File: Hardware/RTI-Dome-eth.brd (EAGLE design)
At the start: 119.4 x 71.1 mm, 78 parts, among them IC1 24AA128ST, IC3 FT232RL, IC5 74LVC245, IC6 74ABT245, J1 POWERPOLE_POWER45A, U1 W5500, X13 PN61729-S, X9 J1011F21PNL

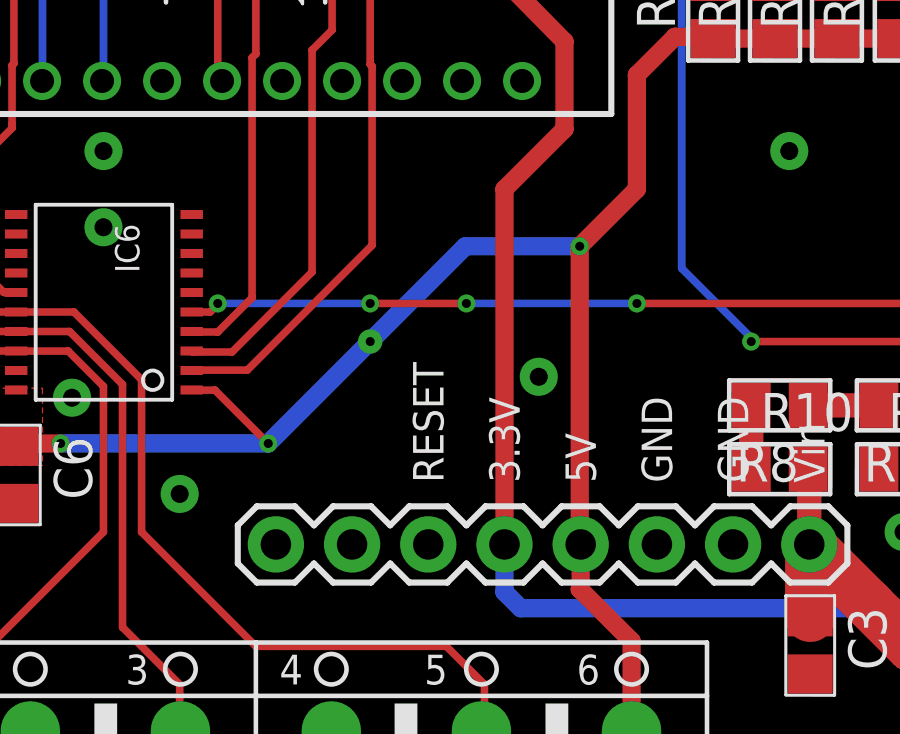
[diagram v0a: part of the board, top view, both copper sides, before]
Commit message: Adding MCP120 for power on reset.
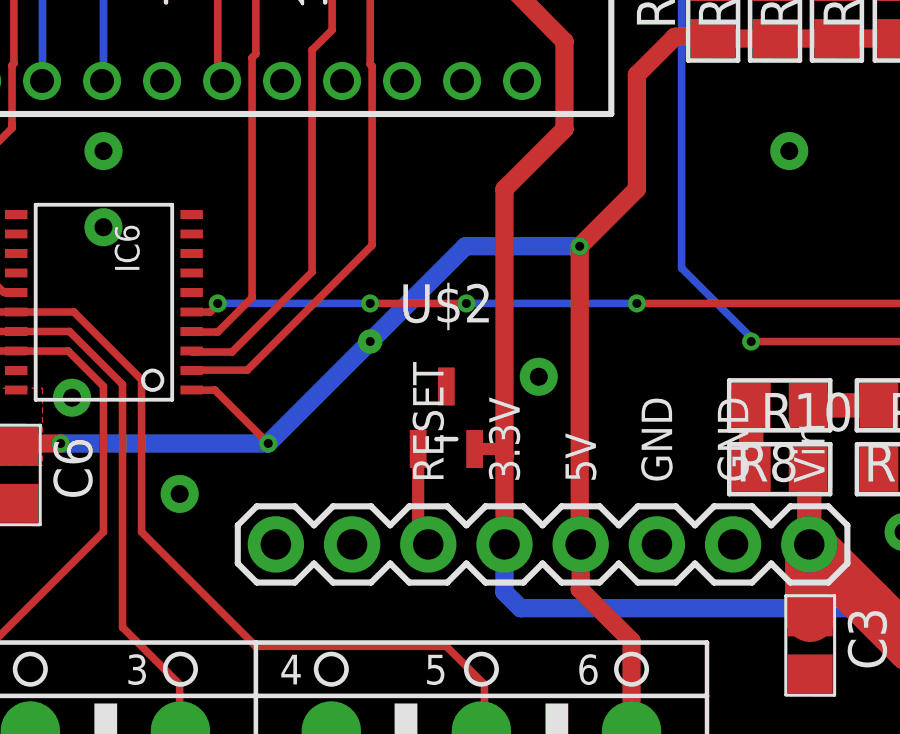
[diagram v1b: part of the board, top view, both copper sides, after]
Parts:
- added U$2: MCP120T-270I_TT, MCP120T-270I_TT:SOT95P237X112-3N
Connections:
- new net RESET: U$1.RESET, U$2.1
- net 3.3V: now also U$2.2
- net GND: now also U$2.3
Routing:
- net RESET: track 0.00 -> 3.32 mm
- net 3.3V: track 350.8 -> 351.9 mm
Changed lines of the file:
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@@
 <layer number="49" name="Reference" color="7" fill="1" visible="yes" active="yes"/>
 <layer number="50" name="dxf" color="7" fill="1" visible="no" active="no"/>
-<layer number="51" name="tDocu" color="7" fill="1" visible="no" active="yes"/>
+<layer number="51" name="tDocu" color="7" fill="1" visible="yes" active="yes"/>
 <layer number="52" name="bDocu" color="7" fill="1" visible="yes" active="yes"/>
 <layer number="53" name="tGND_GNDA" color="7" fill="9" visible="no" active="no"/>
@@
 <element name="C20" library="rti" package="C0805" value="100nF" x="53.34" y="27.94" rot="R90"/>
 <element name="R30" library="rti" package="R0805" value="4.7K" x="58.83275" y="22.86" rot="R270"/>
+<element name="U$2" library="MCP120T-270I_TT" package="SOT95P237X112-3N" value="MCP120T-270I_TT" x="22.86" y="15.24">
+<attribute name="MANUFACTURER_PART_NUMBER" value="MCP120T-270I/TT" x="10.16" y="25.4" size="1.778" layer="27" display="off"/>
+<attribute name="MANUFACTURER_NAME" value="Microchip" x="10.16" y="25.4" size="1.778" layer="27" display="off"/>
+<attribute name="MOUSER_PART_NUMBER" value="579-MCP120T-270I/TT" x="10.16" y="25.4" size="1.778" layer="27" display="off"/>
+<attribute name="DESCRIPTION" value="Microcontroller Supervisory Circuit" x="10.16" y="25.4" size="1.778" layer="27" display="off"/>
+<attribute name="HEIGHT" value="mm" x="10.16" y="25.4" size="1.778" layer="27" display="off"/>
+<attribute name="MOUSER_PRICE-STOCK" value="https://www.mouser.co.uk/ProductDetail/Microchip-Technology/MCP120T-270I-TT?qs=JaP0%252BruNJH91Pwyk6aJdSA%3D%3D" x="10.16" y="25.4" size="1.778" layer="27" display="off"/>
+</element>
 </elements>
 <signals>
@@
 <via x="91.44" y="48.26" extent="1-16" drill="0.6" diameter="1.27"/>
 <via x="91.44" y="44.45" extent="1-16" drill="0.6" diameter="1.27"/>
+<contactref element="U$2" pad="3"/>
 </signal>
 <signal name="+12V" class="1">
@@
 <wire x1="67.33" y1="40.94" x2="67.31" y2="40.96" width="0.254" layer="1"/>
 <wire x1="26.797" y1="24.86025" x2="24.79675" y2="22.86" width="0.6096" layer="1"/>
-<wire x1="24.79675" y1="22.86" x2="24.79675" y2="11.01725" width="0.6096" layer="1"/>
+<wire x1="24.79675" y1="22.86" x2="24.79675" y2="13.97" width="0.6096" layer="1"/>
+<wire x1="24.79675" y1="13.97" x2="24.79675" y2="11.01725" width="0.6096" layer="1"/>
 <wire x1="95.57" y1="24.41575" x2="92.42425" y2="24.41575" width="0.6096" layer="1"/>
 <wire x1="92.42425" y1="24.41575" x2="91.44" y2="25.4" width="0.6096" layer="1"/>
@@
 <wire x1="58.83275" y1="21.91" x2="56.2" y2="21.91" width="0.4064" layer="1"/>
 <wire x1="56.2" y1="21.91" x2="55.88" y2="21.59" width="0.4064" layer="1"/>
+<contactref element="U$2" pad="2"/>
+<wire x1="23.7998" y1="14.1986" x2="24.56815" y2="14.1986" width="0.4064" layer="1"/>
+<wire x1="24.56815" y1="14.1986" x2="24.79675" y2="13.97" width="0.4064" layer="1"/>
 </signal>
 <signal name="RG-11-IN_5V">
@@
 <wire x1="58.1" y1="23.81" x2="58.83275" y2="23.81" width="0.254" layer="1"/>
 </signal>
+<signal name="RESET">
+<contactref element="U$2" pad="1"/>
+<contactref element="U$1" pad="RESET"/>
+<wire x1="21.9202" y1="14.1986" x2="21.9202" y2="11.3538" width="0.4064" layer="1"/>
+<wire x1="21.9202" y1="11.3538" x2="22.25675" y2="11.01725" width="0.4064" layer="1"/>
+</signal>
 </signals>

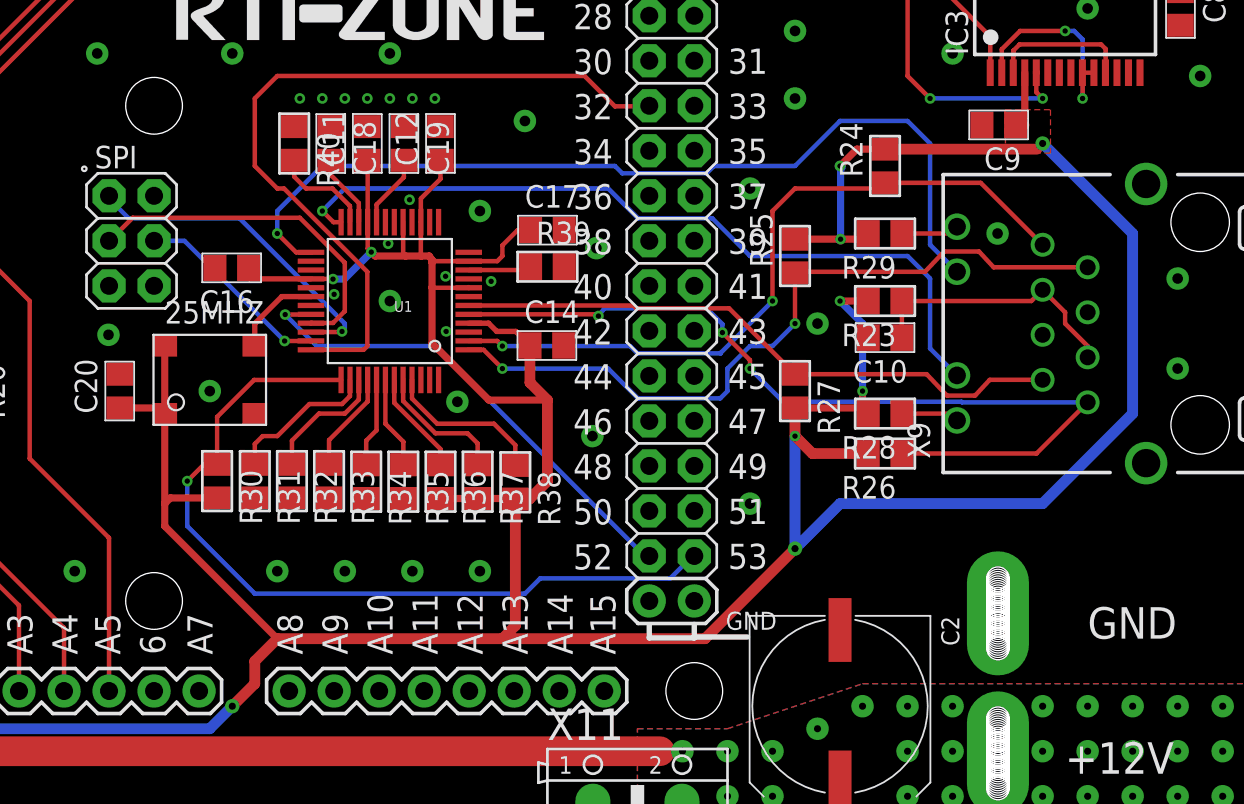
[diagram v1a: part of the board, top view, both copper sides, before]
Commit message: Redid the analog 3.3V on the ethernet shield
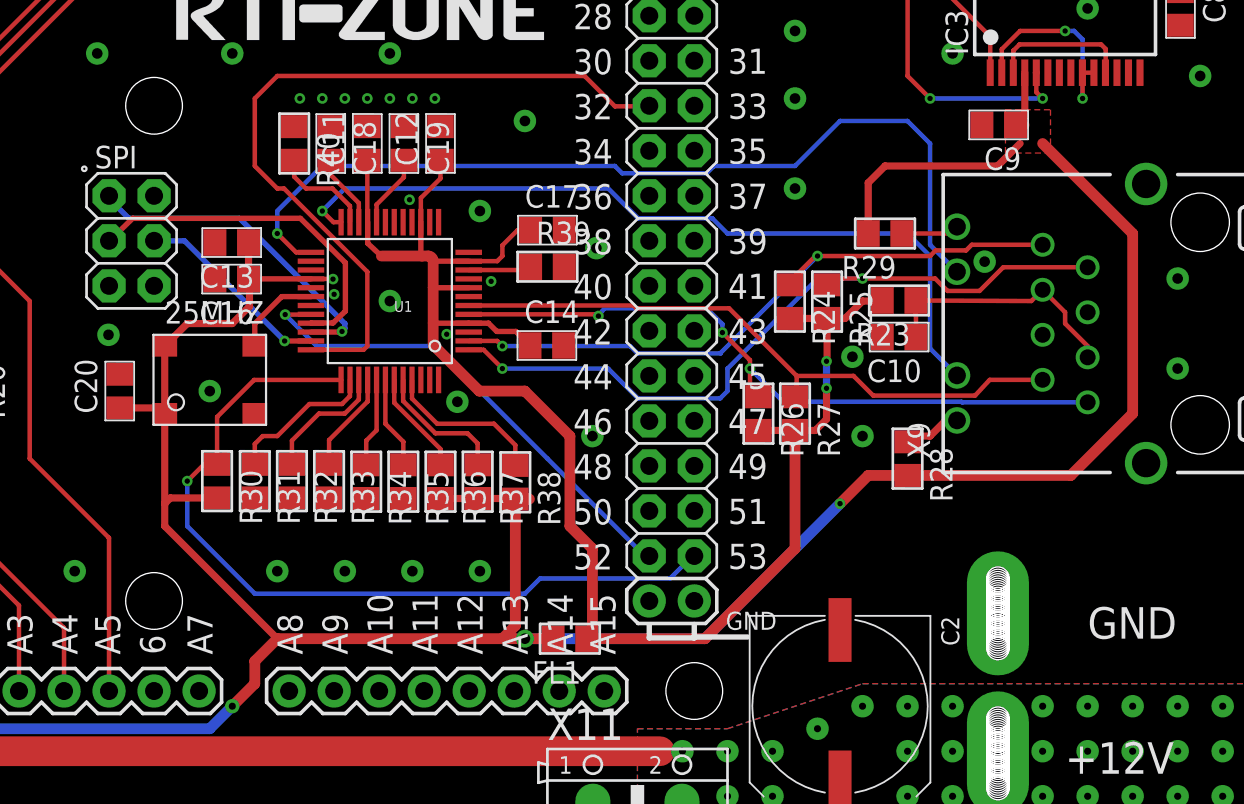
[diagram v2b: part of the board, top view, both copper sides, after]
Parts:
- added C13: 10nF, rti:C0805
- added FL1: BLM21AG121SN1D, BLM21AG121SN1D:L0805
- moved R24 9.35 mm to (91.2, 33.0), turned to 270 degrees
- moved R26 7.49 mm to (89.4, 26.7), turned to 270 degrees
- moved R25 3.14 mm to (93.2, 33.0), turned to 270 degrees
- moved R28 2.84 mm to (97.8, 24.1), turned to 270 degrees
- moved R27 1.27 mm to (91.4, 26.7)
- moved C10 0.79 mm to (97.3, 31.0)
- moved R23 0.79 mm to (97.3, 33.1)
- moved C16 0.64 mm to (59.7, 34.3)
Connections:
- new net AVDD: C11.1, C12.1, C14.1, C17.1, FL1.1, R23.2, R24.2, R25.2, R26.2, R27.2, U1.11, U1.15, U1.17, U1.21, U1.4, U1.8
- net 3.3V: now also C13.1, FL1.2; no longer C11.1, C12.1, C14.1, C17.1, R23.2, R24.2, R25.2, R26.2, R27.2, U1.11, U1.15, U1.17, U1.21, U1.4, U1.8
- net GND: now also C13.2
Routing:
- net AVDD: track 0.00 -> 91.9 mm, vias 0 -> 2
- net 3.3V: track 351.9 -> 275.5 mm, vias 10 -> 4
- net RXN: track 49.6 -> 39.8 mm
- net TXP: track 41.1 -> 37.6 mm
- net RXP: track 35.2 -> 36.1 mm
- net N$7: track 15.1 -> 14.3 mm
- net SPD_100: track 44.3 -> 45.1 mm
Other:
- board text added: "Dome Rotator"

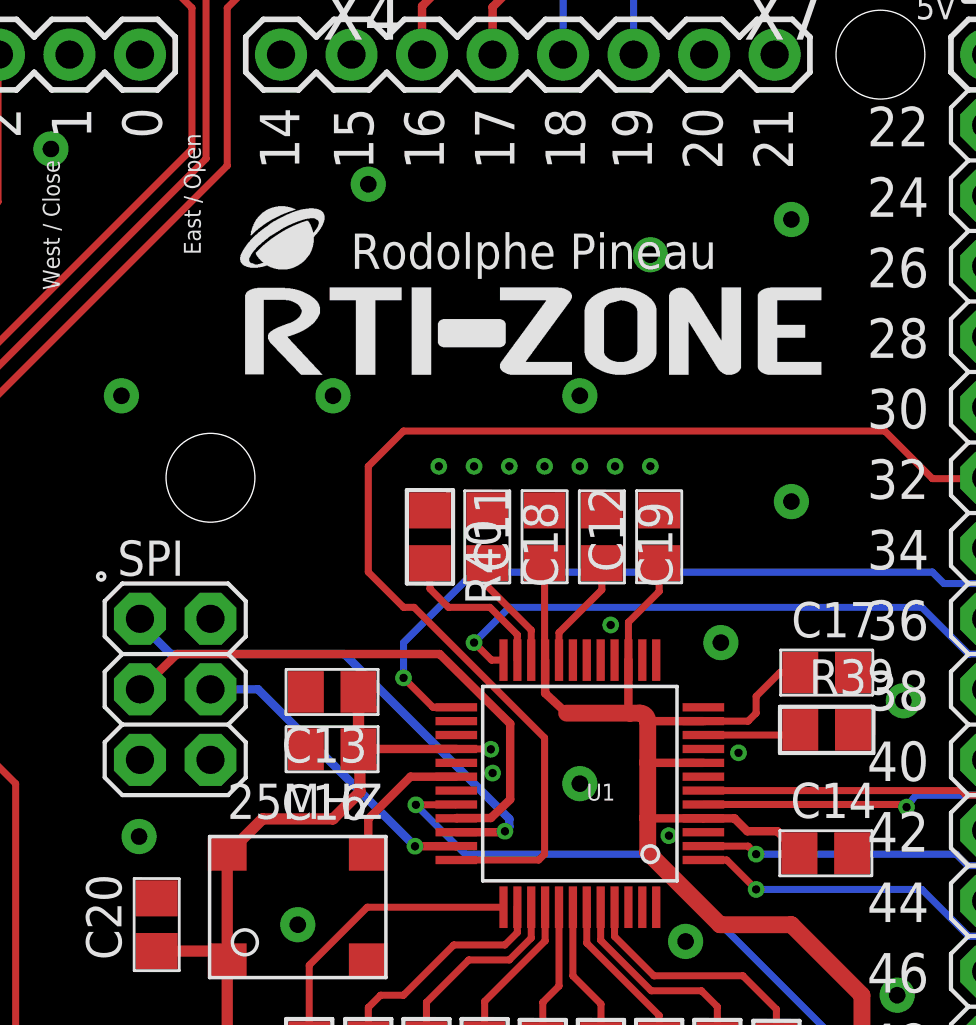
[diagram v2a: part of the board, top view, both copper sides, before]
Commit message: Fix some routing
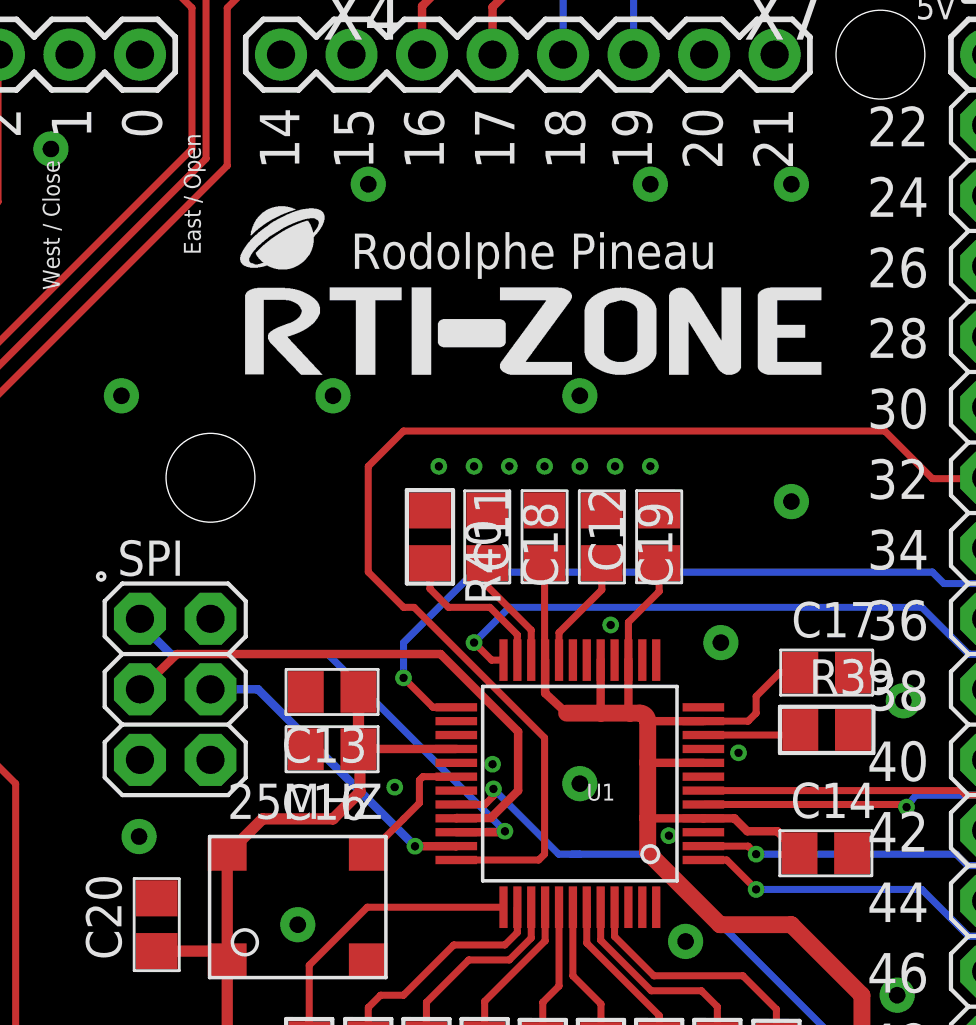
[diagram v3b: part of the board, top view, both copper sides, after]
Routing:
- net ETH_CS: track 27.6 -> 25.7 mm
- net AVDD: track 91.9 -> 93.8 mm
- net 3.3V: track 275.5 -> 274.3 mm, vias 4 -> 3
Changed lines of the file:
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@@
 <via x="52.705" y="31.115" extent="1-16" drill="0.6" diameter="1.27"/>
 <via x="69.69125" y="38.735" extent="1-16" drill="0.3"/>
-<via x="65.43675" y="33.401" extent="1-16" drill="0.3"/>
+<via x="65.43675" y="33.7185" extent="1-16" drill="0.3"/>
 <via x="63.5" y="44.45" extent="1-16" drill="0.3"/>
 <via x="66.04" y="44.45" extent="1-16" drill="0.3"/>
@@
 <via x="59.69" y="46.99" extent="1-16" drill="0.6" diameter="1.27"/>
 <via x="68.58" y="46.99" extent="1-16" drill="0.6" diameter="1.27"/>
-<via x="71.12" y="52.07" extent="1-16" drill="0.6" diameter="1.27"/>
-<via x="76.2" y="53.34" extent="1-16" drill="0.6" diameter="1.27"/>
+<via x="71.12" y="54.61" extent="1-16" drill="0.6" diameter="1.27"/>
+<via x="76.2" y="54.61" extent="1-16" drill="0.6" diameter="1.27"/>
 <via x="52.07" y="46.99" extent="1-16" drill="0.6" diameter="1.27"/>
 <via x="91.44" y="55.88" extent="1-16" drill="0.6" diameter="1.27"/>
@@
 <contactref element="C13" pad="2"/>
 <via x="71.78675" y="31.14675" extent="1-16" drill="0.3"/>
+<via x="61.9125" y="32.893" extent="1-16" drill="0.3"/>
 </signal>
 <signal name="+12V" class="1">
@@
 <contactref element="R37" pad="2"/>
 <contactref element="R36" pad="2"/>
-<wire x1="64.13" y1="34.27" x2="65.298" y2="34.27" width="0.254" layer="1"/>
-<wire x1="65.298" y1="34.27" x2="65.37325" y2="34.25825" width="0.3048" layer="1"/>
-<via x="65.37325" y="34.25825" extent="1-16" drill="0.3"/>
 <wire x1="75.66025" y1="21.8465" x2="75.66025" y2="14.70025" width="0.6096" layer="1"/>
 <wire x1="75.66025" y1="14.70025" x2="74.93" y2="13.97" width="0.6096" layer="1"/>
@@
 <wire x1="52.73675" y1="38.95725" x2="52.73675" y2="38.7985" width="0.3048" layer="16"/>
 <wire x1="52.73675" y1="38.7985" x2="53.848" y2="37.68725" width="0.3048" layer="16"/>
-<wire x1="53.848" y1="37.68725" x2="60.10275" y2="37.68725" width="0.3048" layer="16"/>
-<wire x1="60.10275" y1="37.68725" x2="66.04" y2="31.75" width="0.3048" layer="16"/>
-<wire x1="66.04" y1="31.75" x2="66.04" y2="31.46425" width="0.3048" layer="16"/>
-<wire x1="66.04" y1="31.46425" x2="65.88125" y2="31.3055" width="0.3048" layer="16"/>
 <wire x1="64.13" y1="31.27" x2="65.84575" y2="31.27" width="0.3048" layer="1"/>
 <wire x1="65.84575" y1="31.27" x2="65.88125" y2="31.3055" width="0.3048" layer="1"/>
 <via x="65.88125" y="31.3055" extent="1-16" drill="0.3"/>
+<wire x1="65.2145" y1="31.3055" x2="65.88125" y2="31.3055" width="0.254" layer="16"/>
+<wire x1="53.848" y1="37.68725" x2="59.4995" y2="37.68725" width="0.254" layer="16"/>
+<wire x1="59.4995" y1="37.68725" x2="65.88125" y2="31.3055" width="0.254" layer="16"/>
 </signal>
 <signal name="SCLK">
@@
 <wire x1="52.73675" y1="36.41725" x2="52.7685" y2="36.41725" width="0.3048" layer="1"/>
 <wire x1="52.7685" y1="36.41725" x2="54.07025" y2="37.68725" width="0.3048" layer="1"/>
-<wire x1="54.07025" y1="37.68725" x2="63.53175" y2="37.68725" width="0.3048" layer="1"/>
-<wire x1="66.07175" y1="32.4485" x2="65.37325" y2="31.78175" width="0.3048" layer="1"/>
+<wire x1="54.07025" y1="37.68725" x2="63.5635" y2="37.68725" width="0.3048" layer="1"/>
+<wire x1="66.3575" y1="32.766" x2="65.37325" y2="31.78175" width="0.3048" layer="1"/>
 <wire x1="65.37325" y1="31.78175" x2="64.14175" y2="31.78175" width="0.3048" layer="1"/>
 <wire x1="64.14175" y1="31.78175" x2="64.13" y2="31.77" width="0.3048" layer="1"/>
-<wire x1="66.07175" y1="32.4485" x2="66.07175" y2="35.179" width="0.3048" layer="1"/>
-<wire x1="66.07175" y1="35.179" x2="63.53175" y2="37.68725" width="0.3048" layer="1"/>
+<wire x1="66.3575" y1="32.766" x2="66.3575" y2="34.89325" width="0.3048" layer="1"/>
+<wire x1="66.3575" y1="34.89325" x2="63.5635" y2="37.68725" width="0.3048" layer="1"/>
 </signal>
 <signal name="SDO">
@@
 <wire x1="82.96275" y1="18.63725" x2="77.47" y2="24.13" width="0.254" layer="16"/>
 <wire x1="77.47" y1="24.13" x2="71.12" y2="30.48" width="0.254" layer="16"/>
-<wire x1="71.12" y1="30.48" x2="64.77" y2="30.48" width="0.254" layer="16"/>
-<wire x1="64.77" y1="30.48" x2="64.4525" y2="30.48" width="0.254" layer="16"/>
-<wire x1="64.4525" y1="30.48" x2="62.6745" y2="32.258" width="0.254" layer="16"/>
-<via x="62.6745" y="32.258" extent="1-16" drill="0.3"/>
-<wire x1="62.6745" y1="32.258" x2="64.118" y2="32.258" width="0.254" layer="1"/>
-<wire x1="64.118" y1="32.258" x2="64.13" y2="32.27" width="0.254" layer="1"/>
+<wire x1="71.12" y1="30.48" x2="68.58" y2="30.48" width="0.254" layer="16"/>
+<via x="65.4685" y="32.8295" extent="1-16" drill="0.3"/>
+<wire x1="68.58" y1="30.48" x2="68.2625" y2="30.48" width="0.254" layer="16"/>
+<wire x1="65.4685" y1="32.8295" x2="67.818" y2="30.48" width="0.254" layer="16"/>
+<wire x1="67.818" y1="30.48" x2="68.58" y2="30.48" width="0.254" layer="16"/>
+<wire x1="64.13" y1="32.27" x2="65.163" y2="32.27" width="0.254" layer="1"/>
+<wire x1="65.163" y1="32.27" x2="65.2145" y2="32.3215" width="0.254" layer="1"/>
+<wire x1="65.2145" y1="32.3215" x2="65.4685" y2="32.5755" width="0.254" layer="1"/>
+<wire x1="65.4685" y1="32.5755" x2="65.4685" y2="32.8295" width="0.254" layer="1"/>
 </signal>
 <signal name="SPD_100">
@@
 <contactref element="U1" pad="30"/>
 <contactref element="25MHZ" pad="3"/>
-<wire x1="64.13" y1="33.27" x2="62.48" y2="33.27" width="0.3048" layer="1"/>
-<wire x1="62.48" y1="33.27" x2="60.96" y2="31.75" width="0.3048" layer="1"/>
-<wire x1="60.96" y1="31.75" x2="60.96" y2="30.48" width="0.3048" layer="1"/>
+<wire x1="64.13" y1="33.27" x2="62.9245" y2="33.27" width="0.254" layer="1"/>
+<wire x1="62.9245" y1="33.27" x2="62.8015" y2="33.147" width="0.254" layer="1"/>
+<wire x1="62.8015" y1="33.147" x2="62.8015" y2="32.3215" width="0.254" layer="1"/>
+<wire x1="62.8015" y1="32.3215" x2="62.23" y2="31.75" width="0.254" layer="1"/>
+<wire x1="62.23" y1="31.75" x2="60.96" y2="30.48" width="0.254" layer="1"/>
 </signal>
 <signal name="XO">
@@
 <wire x1="71.02475" y1="31.78175" x2="71.02475" y2="33.782" width="0.6096" layer="1"/>
 <wire x1="71.02475" y1="33.782" x2="71.02475" y2="35.27425" width="0.6096" layer="1"/>
-<wire x1="68.10375" y1="35.56" x2="70.38975" y2="35.56" width="0.6096" layer="1"/>
+<wire x1="68.10375" y1="35.56" x2="69.342" y2="35.56" width="0.6096" layer="1"/>
+<wire x1="69.342" y1="35.56" x2="70.38975" y2="35.56" width="0.6096" layer="1"/>
 <wire x1="70.38975" y1="35.56" x2="70.739" y2="35.56" width="0.6096" layer="1"/>
 <wire x1="70.739" y1="35.56" x2="71.02475" y2="35.27425" width="0.6096" layer="1" curve="-90"/>
-<wire x1="70.33" y1="37.47" x2="69.33" y2="37.47" width="0" layer="19" extent="1-1"/>
+<wire x1="69.33" y1="37.47" x2="69.33" y2="35.572" width="0.3048" layer="1"/>
+<wire x1="69.33" y1="35.572" x2="69.342" y2="35.56" width="0.3048" layer="1"/>
 </signal>
 </signals>
